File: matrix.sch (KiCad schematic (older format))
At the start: 24 parts

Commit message: Ready for prototyping
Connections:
- no-connect marks 0 -> 24
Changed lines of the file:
@@
 Text HLabel 4850 1300 0    50   Input ~ 0
 COL_3
+NoConn ~ 3050 2050
+NoConn ~ 3150 1950
+NoConn ~ 3600 2050
+NoConn ~ 3700 1950
+NoConn ~ 4150 2050
+NoConn ~ 4250 1950
+NoConn ~ 4700 2050
+NoConn ~ 4800 1950
+NoConn ~ 4800 2900
+NoConn ~ 4700 3000
+NoConn ~ 4250 2900
+NoConn ~ 4150 3000
+NoConn ~ 3700 2900
+NoConn ~ 3600 3000
+NoConn ~ 3150 2900
+NoConn ~ 3050 3000
+NoConn ~ 3150 3850
+NoConn ~ 3050 3950
+NoConn ~ 3600 3950
+NoConn ~ 3700 3850
+NoConn ~ 4150 3950
+NoConn ~ 4250 3850
+NoConn ~ 4700 3950
+NoConn ~ 4800 3850
 $EndSCHEMATC

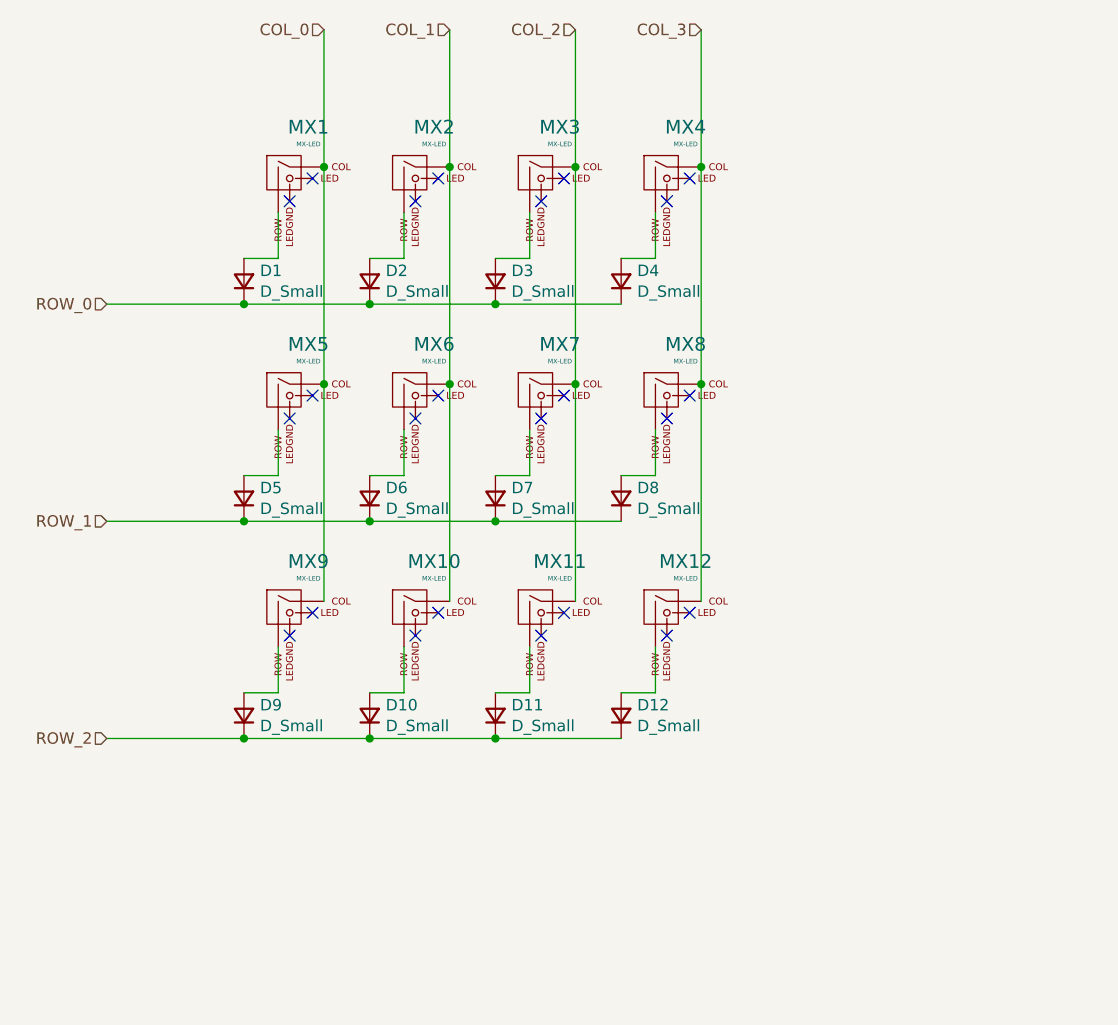
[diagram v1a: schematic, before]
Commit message: Adds single color backlighting to each key :)
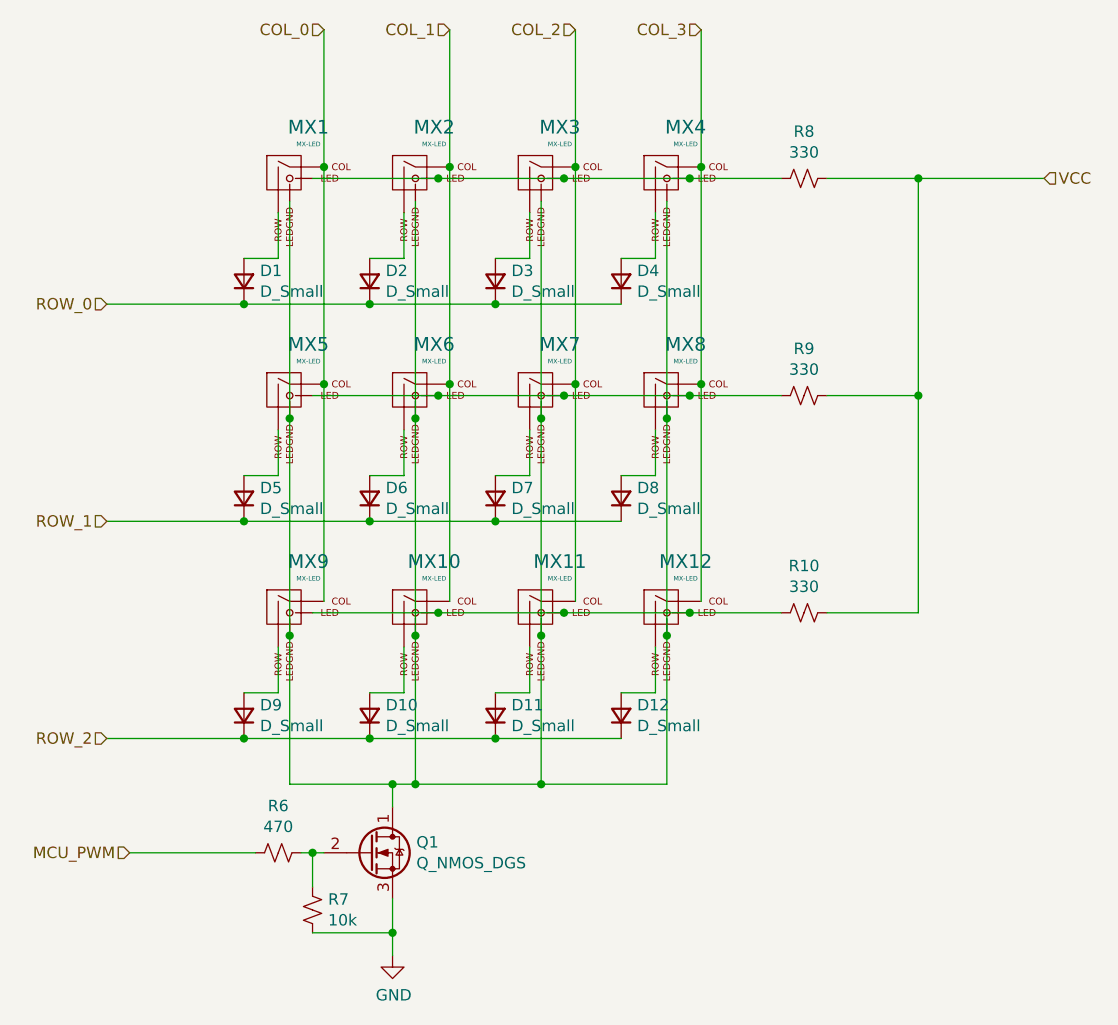
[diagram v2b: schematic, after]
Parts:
- added Q1: Q_NMOS_DGS, Package_TO_SOT_SMD:SOT-723, symbol Device:Q_NMOS_DGS
- added R10, R8, R9: 330, Resistor_SMD:R_0805_2012Metric, symbol Device:R_Small_US
- added R6: 470, Resistor_SMD:R_0805_2012Metric, symbol Device:R_Small_US
- added R7: 10k, Resistor_SMD:R_0805_2012Metric, symbol Device:R_Small_US
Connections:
- net at MX12.3 (LED): now also MX10.3 (LED), MX11.3 (LED), MX9.3 (LED), R10.2
- net at MX12.4 (LEDGND): now also MX1.4 (LEDGND), MX10.4 (LEDGND), MX11.4 (LEDGND), MX2.4 (LEDGND), MX3.4 (LEDGND), MX4.4 (LEDGND), MX5.4 (LEDGND), MX6.4 (LEDGND), MX7.4 (LEDGND), MX8.4 (LEDGND), MX9.4 (LEDGND), Q1.1 (D)
- net at MX8.3 (LED): now also MX5.3 (LED), MX6.3 (LED), MX7.3 (LED), R9.2
- net at MX4.3 (LED): now also MX1.3 (LED), MX2.3 (LED), MX3.3 (LED), R8.2
- new net: Q1.2 (G), R6.1, R7.1
- new net GND: Q1.3 (S), R7.2
- new net MCU_PWM: R6.2
- new net VCC: R10.1, R8.1, R9.1
- no-connect marks 24 -> 0
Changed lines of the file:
@@
 Connection ~ 3200 2850
-Wire Wire Line
-	3200 2850 3200 1900
 Wire Wire Line
 	3750 3800 3750 2850
@@
 Text HLabel 4850 1300 0    50   Input ~ 0
 COL_3
-NoConn ~ 3050 2050
-NoConn ~ 3150 1950
-NoConn ~ 3600 2050
-NoConn ~ 3700 1950
-NoConn ~ 4150 2050
-NoConn ~ 4250 1950
-NoConn ~ 4700 2050
-NoConn ~ 4800 1950
-NoConn ~ 4800 2900
-NoConn ~ 4700 3000
-NoConn ~ 4250 2900
-NoConn ~ 4150 3000
-NoConn ~ 3700 2900
-NoConn ~ 3600 3000
-NoConn ~ 3150 2900
-NoConn ~ 3050 3000
-NoConn ~ 3150 3850
-NoConn ~ 3050 3950
-NoConn ~ 3600 3950
-NoConn ~ 3700 3850
-NoConn ~ 4150 3950
-NoConn ~ 4250 3850
-NoConn ~ 4700 3950
-NoConn ~ 4800 3850
+$Comp
+L Device:R_Small_US R6
+U 1 1 5F6B32D8
+P 3000 4900
+F 0 "R6" V 2795 4900 50  0000 C CNN
+F 1 "470" V 2886 4900 50  0000 C CNN
+F 2 "Resistor_SMD:R_0805_2012Metric" H 3000 4900 50  0001 C CNN
+F 3 "~" H 3000 4900 50  0001 C CNN
+	1    3000 4900
+	0    1    1    0
+$EndComp
+Wire Wire Line
+	3200 4900 3150 4900
+Text HLabel 2350 4900 0    50   Input ~ 0
+MCU_PWM
+Wire Wire Line
+	3150 4900 3150 5050
+Connection ~ 3150 4900
+Wire Wire Line
+	3150 4900 3100 4900
+$Comp
+L Device:R_Small_US R7
+U 1 1 5F6B8038
+P 3150 5150
+F 0 "R7" H 3218 5196 50  0000 L CNN
+F 1 "10k" H 3218 5105 50  0000 L CNN
+F 2 "Resistor_SMD:R_0805_2012Metric" H 3150 5150 50  0001 C CNN
+F 3 "~" H 3150 5150 50  0001 C CNN
+	1    3150 5150
+	1    0    0    -1
+$EndComp
+Wire Wire Line
+	3150 5250 3500 5250
+Wire Wire Line
+	3500 5250 3500 5350
+$Comp
+L power:GND #PWR0121
+U 1 1 5F6B99E7
+P 3500 5350
+F 0 "#PWR0121" H 3500 5100 50  0001 C CNN
+F 1 "GND" H 3505 5177 50  0000 C CNN
+F 2 "" H 3500 5350 50  0001 C CNN
+F 3 "" H 3500 5350 50  0001 C CNN
+	1    3500 5350
+	1    0    0    -1
+$EndComp
+Wire Wire Line
+	3500 5100 3500 5250
+Connection ~ 3500 5250
+Wire Wire Line
+	3050 4600 3500 4600
+Wire Wire Line
+	3500 4600 3500 4700
+Wire Wire Line
+	3050 2050 3050 3000
+Connection ~ 3050 3000
+Wire Wire Line
+	3050 3000 3050 3950
+Connection ~ 3050 3950
+Wire Wire Line
+	3050 3950 3050 4600
+Wire Wire Line
+	3600 2050 3600 3000
+Connection ~ 3600 3000
+Wire Wire Line
+	3600 3000 3600 3950
+Connection ~ 3600 3950
+Wire Wire Line
+	3600 3950 3600 4600
+Connection ~ 3500 4600
+Wire Wire Line
+	4150 2050 4150 3000
+Wire Wire Line
+	3500 4600 3600 4600
+Connection ~ 4150 3000
+Wire Wire Line
+	4150 3000 4150 3950
+Connection ~ 4150 3950
+Wire Wire Line
+	4150 3950 4150 4600
+Connection ~ 3600 4600
+Wire Wire Line
+	4700 2050 4700 3000
+Wire Wire Line
+	3600 4600 4150 4600
+Connection ~ 4700 3000
+Wire Wire Line
+	4700 3000 4700 3950
+Connection ~ 4700 3950
+Wire Wire Line
+	4700 3950 4700 4600
+Connection ~ 4150 4600
+Wire Wire Line
+	4150 4600 4700 4600
+Wire Wire Line
+	3200 2850 3200 1900
+Connection ~ 3700 1950
+Wire Wire Line
+	3700 1950 3150 1950
+Connection ~ 4250 1950
+Wire Wire Line
+	4250 1950 3700 1950
+Wire Wire Line
+	4800 1950 4250 1950
+Wire Wire Line
+	3150 2900 3700 2900
+Connection ~ 3700 2900
+Wire Wire Line
+	3700 2900 4250 2900
+Connection ~ 4250 2900
+Wire Wire Line
+	4250 2900 4800 2900
+Wire Wire Line
+	3150 3850 3700 3850
+Connection ~ 3700 3850
+Wire Wire Line
+	3700 3850 4250 3850
+Connection ~ 4250 3850
+Wire Wire Line
+	4250 3850 4800 3850
+Text HLabel 6350 1950 2    50   Input ~ 0
+VCC
+Wire Wire Line
+	2900 4900 2350 4900
+$Comp
+L Device:Q_NMOS_DGS Q1
+U 1 1 5F70697E
+P 3400 4900
+F 0 "Q1" H 3604 4946 50  0000 L CNN
+F 1 "Q_NMOS_DGS" H 3604 4855 50  0000 L CNN
+F 2 "Package_TO_SOT_SMD:SOT-723" H 3600 5000 50  0001 C CNN
+F 3 "~" H 3400 4900 50  0001 C CNN
+	1    3400 4900
+	1    0    0    -1
+$EndComp
+Wire Wire Line
+	5800 1950 5800 2900
+$Comp
+L Device:R_Small_US R8
+U 1 1 5F71A036
+P 5300 1950
+F 0 "R8" V 5095 1950 50  0000 C CNN
+F 1 "330" V 5186 1950 50  0000 C CNN
+F 2 "Resistor_SMD:R_0805_2012Metric" H 5300 1950 50  0001 C CNN
+F 3 "~" H 5300 1950 50  0001 C CNN
+	1    5300 1950
+	0    1    1    0
+$EndComp
+$Comp
+L Device:R_Small_US R9
+U 1 1 5F71B2D4
+P 5300 2900
+F 0 "R9" V 5095 2900 50  0000 C CNN
+F 1 "330" V 5186 2900 50  0000 C CNN
+F 2 "Resistor_SMD:R_0805_2012Metric" H 5300 2900 50  0001 C CNN
+F 3 "~" H 5300 2900 50  0001 C CNN
+	1    5300 2900
+	0    1    1    0
+$EndComp
+$Comp
+L Device:R_Small_US R10
+U 1 1 5F71B92D
+P 5300 3850
+F 0 "R10" V 5095 3850 50  0000 C CNN
+F 1 "330" V 5186 3850 50  0000 C CNN
+F 2 "Resistor_SMD:R_0805_2012Metric" H 5300 3850 50  0001 C CNN
+F 3 "~" H 5300 3850 50  0001 C CNN
+	1    5300 3850
+	0    1    1    0
+$EndComp
+Wire Wire Line
+	5400 1950 5800 1950
+Connection ~ 5800 1950
+Wire Wire Line
+	5800 1950 6350 1950
+Wire Wire Line
+	5200 1950 4800 1950
+Connection ~ 4800 1950
+Wire Wire Line
+	4800 2900 5200 2900
+Connection ~ 4800 2900
+Wire Wire Line
+	5400 2900 5800 2900
+Connection ~ 5800 2900
+Wire Wire Line
+	5800 2900 5800 3850
+Wire Wire Line
+	5800 3850 5400 3850
+Wire Wire Line
+	5200 3850 4800 3850
+Connection ~ 4800 3850
 $EndSCHEMATC
